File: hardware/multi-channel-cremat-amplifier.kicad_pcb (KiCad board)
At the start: 2 copper layers, 225 x 235 mm, 221 parts, among them J1 MCX CONMCX013, J10 MCX CONMCX013, J11 MCX CONMCX013, J12 MCX CONMCX013, J13 MCX CONMCX013, J14 MCX CONMCX013, J15 MCX CONMCX013, J16 MCX CONMCX013, J17 MCX CONMCX013, J18 MCX CONMCX013, J19 MCX CONMCX013, J2 MCX CONMCX013, J20 MCX CONMCX013, J21 MCX CONMCX013, J22 MCX CONMCX013, J23 MCX CONMCX013, J24 MCX CONMCX013, J25 MCX CONMCX013, J26 MCX CONMCX013, J27 MCX CONMCX013, J28 MCX CONMCX013, J29 MCX CONMCX013, J3 MCX CONMCX013, J30 MCX CONMCX013, J31 MCX CONMCX013, J32 MCX CONMCX013, J33 MCX CONMCX013, J34 MCX CONMCX013, J35 MCX CONMCX013, J36 MCX CONMCX013, J4 MCX CONMCX013, J5 MCX CONMCX013, J6 MCX CONMCX013, J7 MCX CONMCX013, J8 MCX CONMCX013, J9 MCX CONMCX013, U1 CR-112, U10 CR-200-1us, U11 CR-210, U12 EL5167, U13 CR-112, U14 CR-200-1us, U15 CR-210, U16 EL5167, U17 CR-112, U18 CR-200-1us, U19 CR-210, U2 CR-200-1us, U20 EL5167, U21 CR-112, U22 CR-200-1us, U23 CR-210, U24 EL5167, U25 CR-112, U26 CR-200-1us, U27 CR-210, U28 EL5167, U29 CR-112, U3 CR-210, U30 CR-200-1us, U31 CR-210, U32 EL5167, U33 CR-112, U34 CR-200-1us, U35 CR-210, U36 EL5167, U37 CR-112, U38 CR-200-1us, U39 CR-210, U4 EL5167, U40 EL5167, U41 CR-112, U42 CR-200-1us, U43 CR-210, U44 EL5167, U45 CR-112, U46 CR-200-1us, U47 CR-210, U48 EL5167, U5 CR-112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

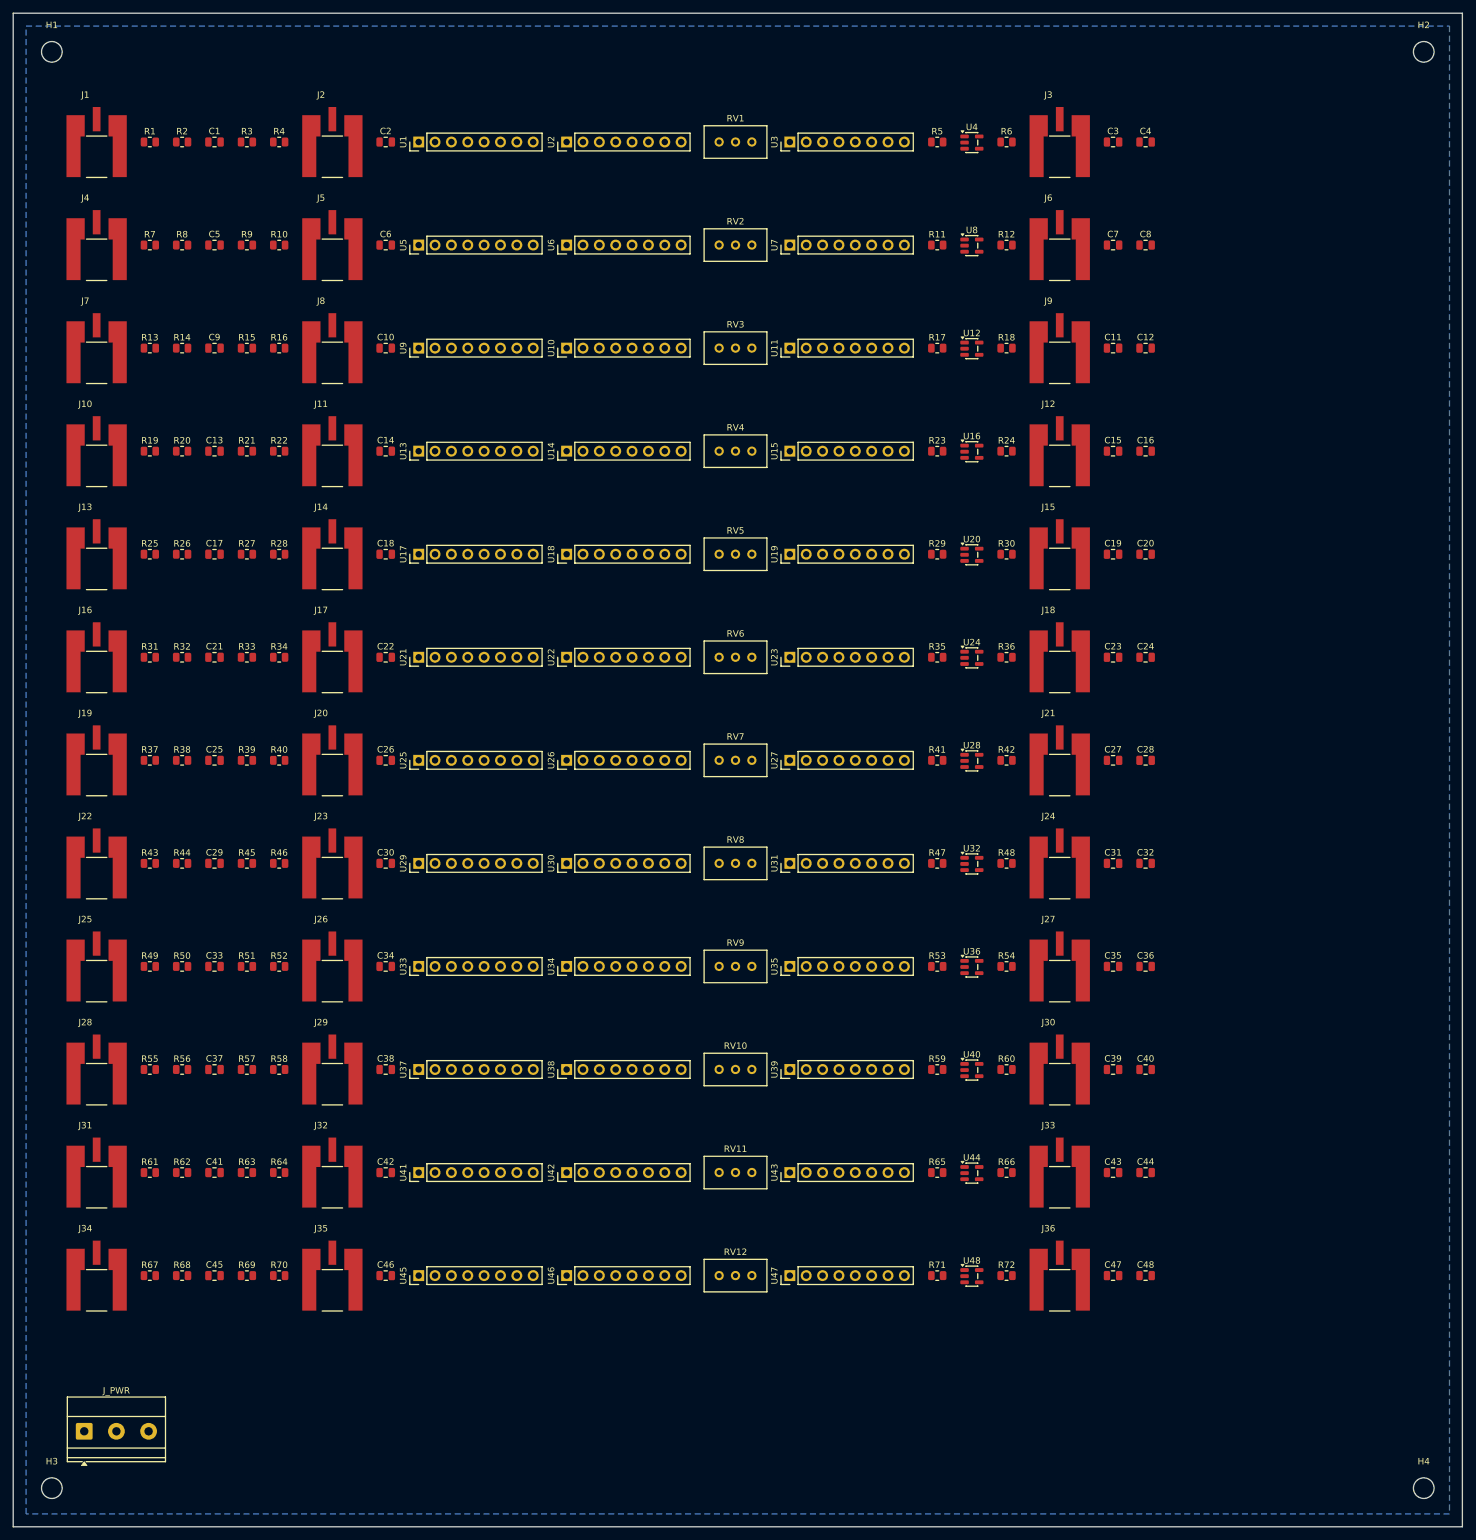
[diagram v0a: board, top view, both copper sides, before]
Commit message: Track 6 DONE: fully autorouted 12-channel board, DRC 0/0/0
Did the complete layout headless -- placement + routing + planes:
- gen_pcb.py: 4-layer board, GND plane (In1) + -VDC plane (In2) so both
  outer layers are free to route; bbox-packed per-channel rows (DRC-clean
  placement).
- export_dsn.py -> Specctra DSN -> FreeRouting v2.2.4 (Java 25) autoroutes
  all 480 nets (0 unrouted) -> import_ses.py -> routed .kicad_pcb.
- fill_zones.py: fill GND/-VDC planes + add outer-layer GND ground-fill,
  solid pad connection (reconnects stray THT GND pads, no starved thermals).

Final DRC: 0 errors, 0 warnings, 0 unconnected. 1070 track segments.
Render: hardware/routed-top.png (12 clean channel rows). Fab outputs
(gerbers/drill/pos, gitignored) export cleanly from the routed board.

Recipe documented in docs/FREEROUTING.md; status synced in development-plan.
(2-layer left ~9 -VDC unrouted; the GND+-VDC planes on 4 layers fixed it.)
GUI polish only: restore MCX Edge.Cuts cutouts (parked on Dwgs.User) when
fixing jacks to the board edge.

Co-Authored-By: Claude Opus 4.8 <noreply@anthropic.com>
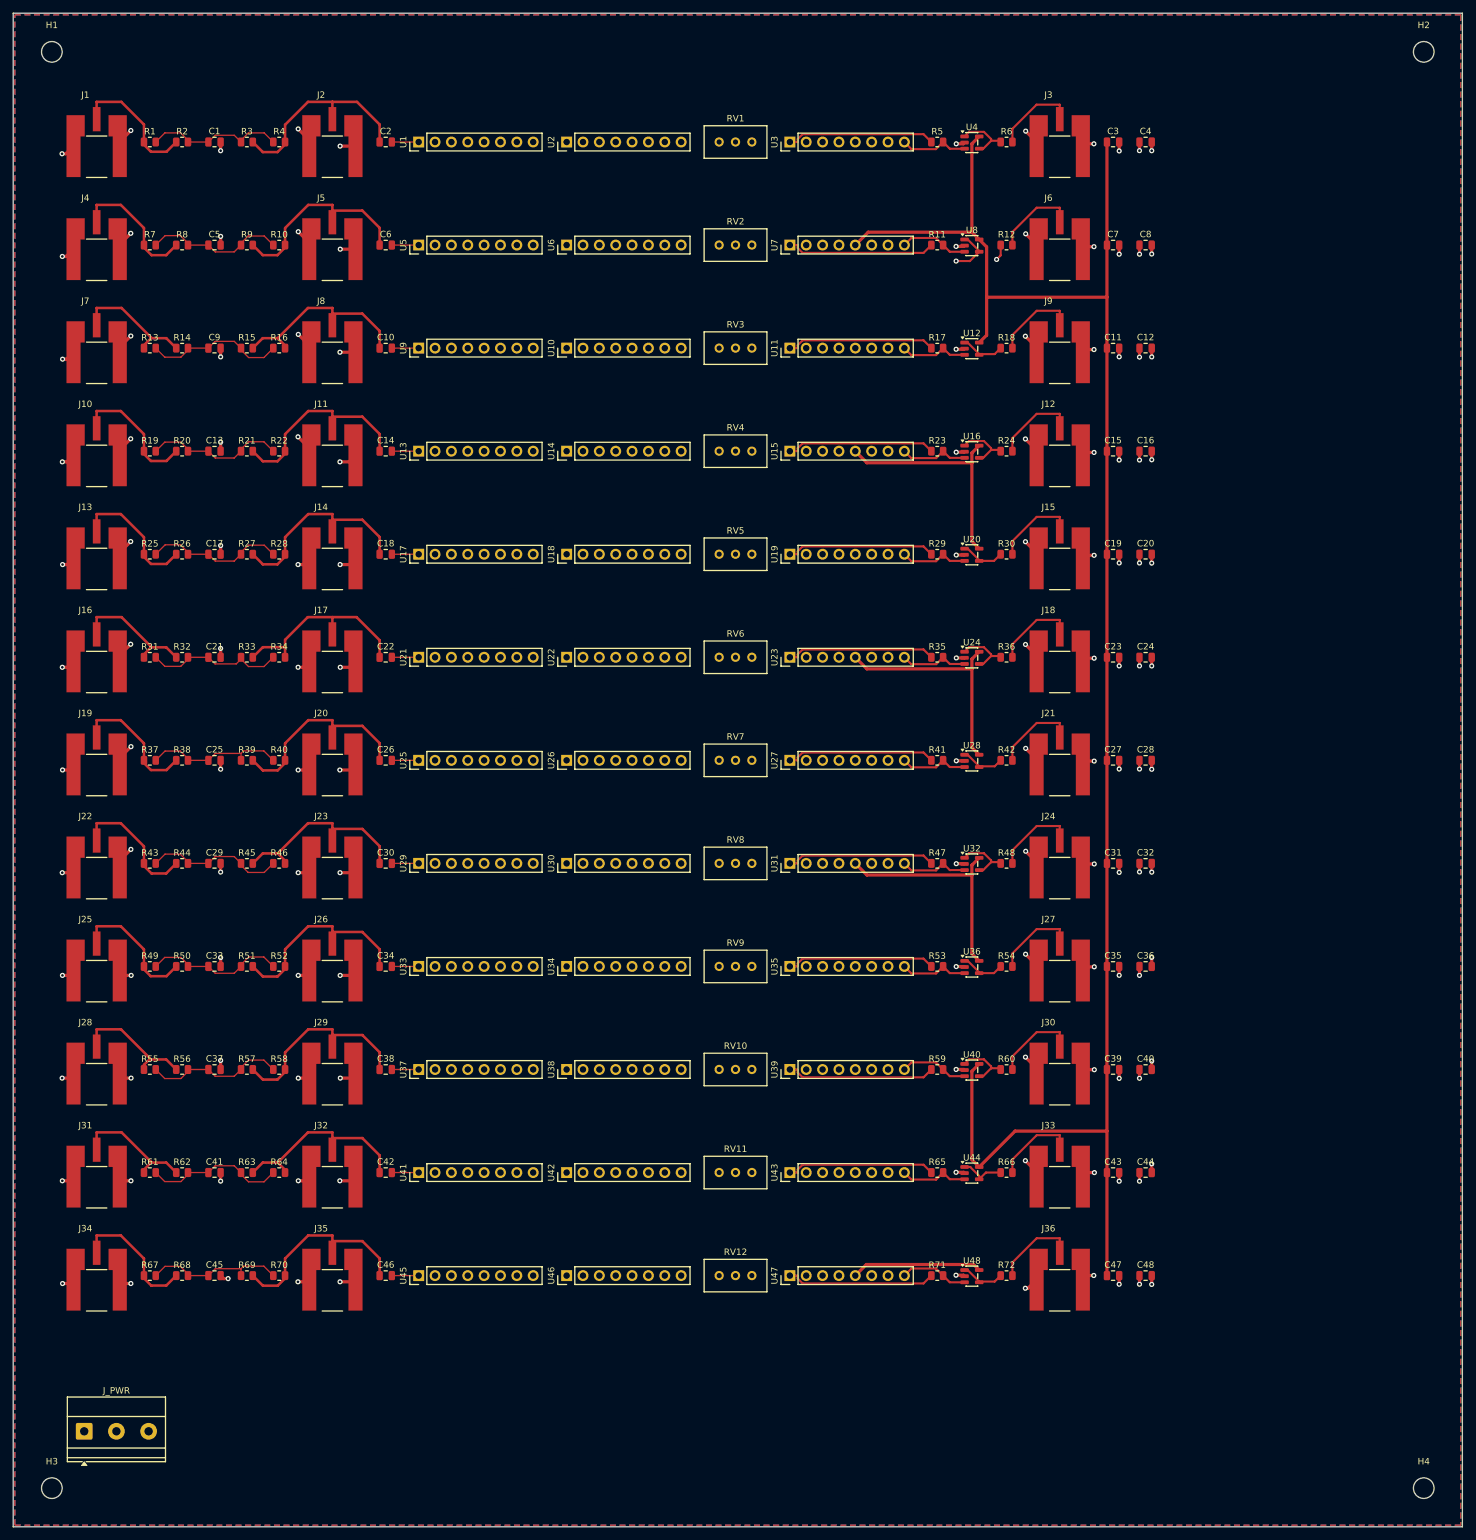
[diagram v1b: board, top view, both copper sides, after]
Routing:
- net +VDC: track 0.00 -> 1074.8 mm
- net GND: track 0.00 -> 231.6 mm, vias 0 -> 108
- net /ch12/SH_OUT: track 0.00 -> 41.1 mm
- net /ch2/SH_OUT: track 0.00 -> 41.1 mm
- net /ch11/SH_OUT: track 0.00 -> 41.1 mm
- net /ch10/SH_OUT: track 0.00 -> 41.1 mm
- net /ch7/SH_OUT: track 0.00 -> 41.1 mm
- net /ch4/SH_OUT: track 0.00 -> 41.1 mm
- net /ch1/SH_OUT: track 0.00 -> 41.0 mm
- net /ch3/SH_OUT: track 0.00 -> 41.0 mm
- net /ch9/SH_OUT: track 0.00 -> 41.0 mm
- net /ch6/SH_OUT: track 0.00 -> 41.0 mm
- net /ch8/SH_OUT: track 0.00 -> 41.0 mm
- net /ch5/SH_OUT: track 0.00 -> 41.0 mm
- net -VDC: track 0.00 -> 32.4 mm, vias 0 -> 24
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- added copper zone on In2.Cu, net -VDC
- added copper zone on F.Cu, net GND
- added copper zone on In1.Cu, net GND
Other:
- copper layers 2 -> 4
